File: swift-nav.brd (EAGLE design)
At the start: 53 x 53 mm, 171 parts, among them J1 SMA_EDGE, J6 ZX62-B-5PA, Q1 MOSFET-PCHANNELSMD, U1 6SLX9FTG256, U10 MAX2769, U12 PT7M8206B33TA5EX, U13 M25PX80, U2 LTC3407A_DFN, U3 STM32-M-64-LQFP, U4 7Q-16.368MBG-T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

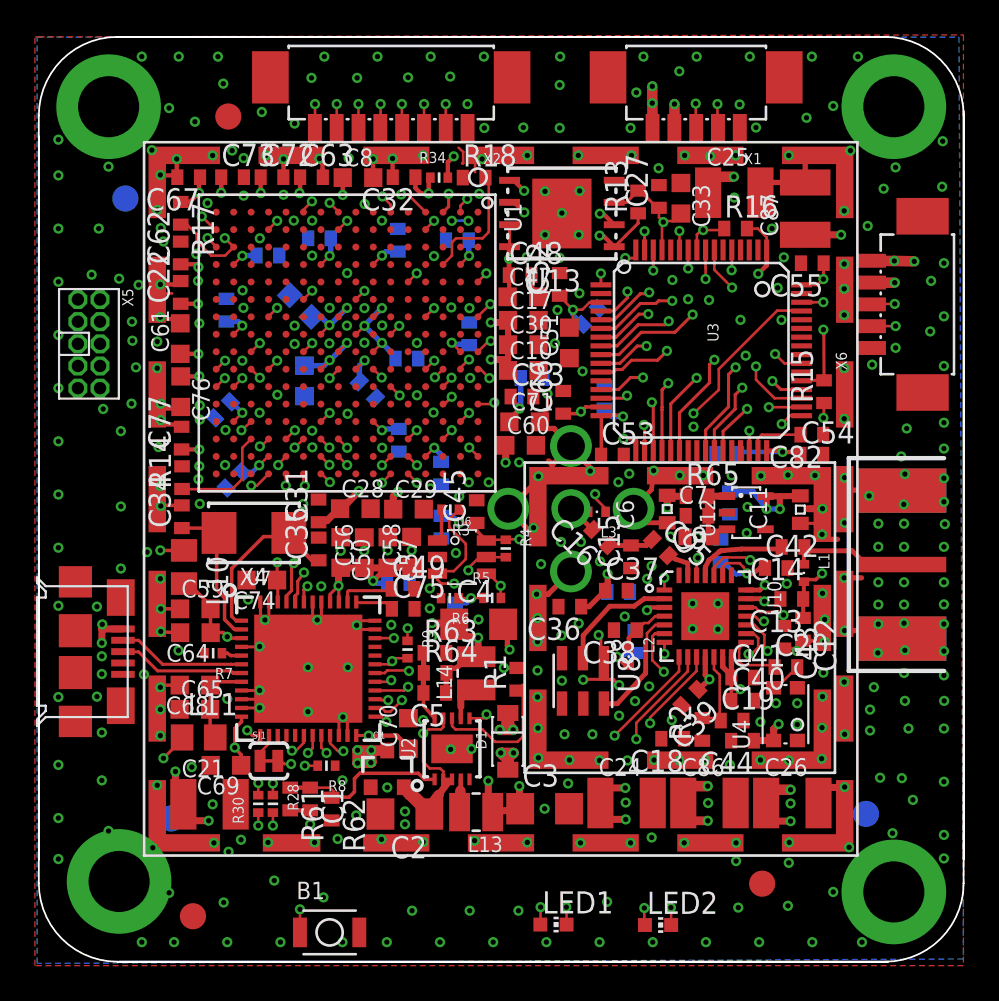
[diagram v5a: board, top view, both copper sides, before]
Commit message: Changed hole separation to 43.8mm
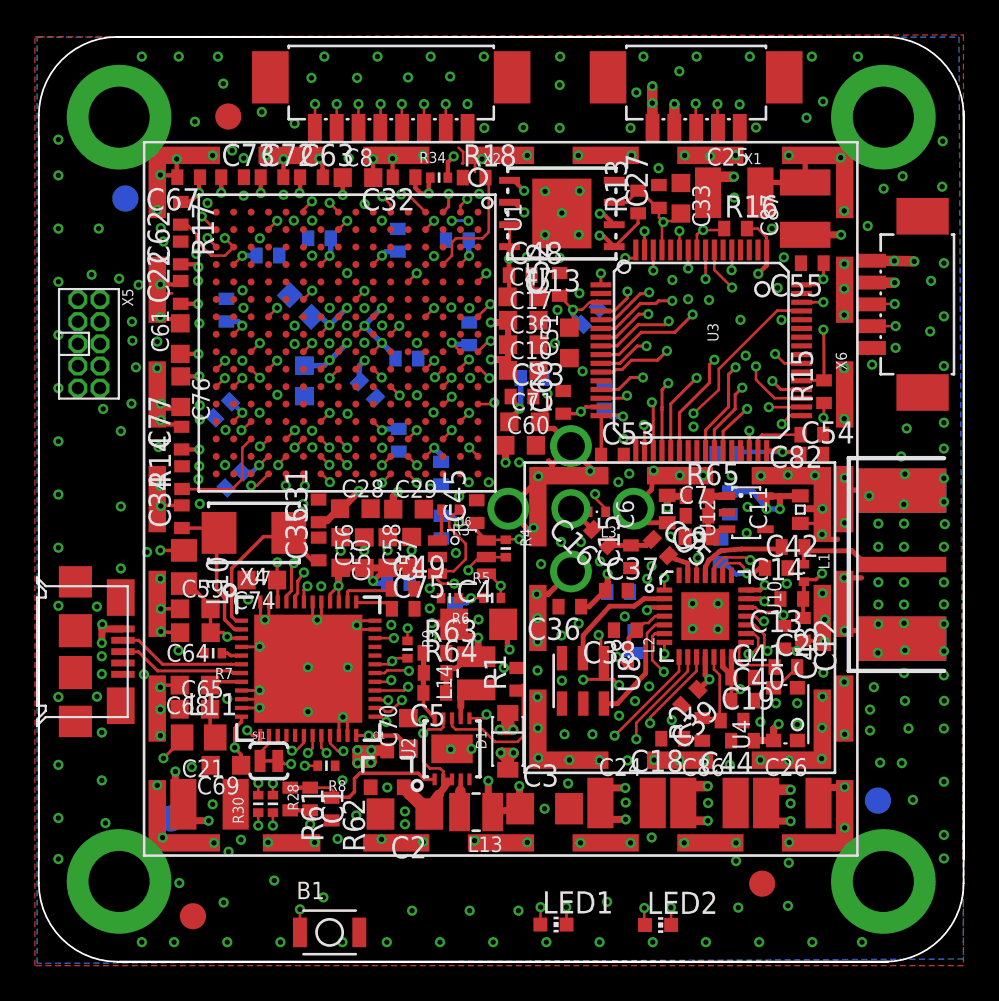
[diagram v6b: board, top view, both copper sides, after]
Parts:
- moved JP5 1.03 mm to (51.5, 12.6)
- moved H4 0.85 mm to (51.8, 51.8)
- moved H2 0.85 mm to (51.8, 8.00)
- moved H3 0.85 mm to (8.00, 51.8)
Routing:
- net N$39: track 62.6 -> 63.6 mm
- net N$59: track 56.9 -> 57.6 mm
- net GND: vias 403 -> 398
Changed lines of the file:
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@@
 <element name="R28" library="pel_dipol_comp" package="0402-RES" value="150" x="16.8148" y="12.446" rot="R270"/>
 <element name="R30" library="pel_dipol_comp" package="0402-RES" value="150" x="15.9766" y="12.446" rot="R90"/>
-<element name="JP5" library="aspirin" package="FIDUCIAL-1.5X3" value="FIDUCIAL1.5X3" x="50.804" y="11.872" rot="MR180"/>
+<element name="JP5" library="aspirin" package="FIDUCIAL-1.5X3" value="FIDUCIAL1.5X3" x="51.4898" y="12.634" rot="MR180"/>
 <element name="JP6" library="aspirin" package="FIDUCIAL-1.5X3" value="FIDUCIAL1.5X3" x="8.3586" y="47.138" rot="MR270"/>
 <element name="JP7" library="aspirin" package="FIDUCIAL-1.5X3" value="FIDUCIAL1.5X3" x="10.984" y="11.61" rot="MR270"/>
@@
 <element name="X2" library="pel_molex" package="PB-53261-08" value="" x="23.5966" y="52.2832" rot="R180"/>
 <element name="C74" library="rcl" package="C0603K" value="0.047uF" x="16.1798" y="25.273" rot="R180"/>
-<element name="H2" library="swift-nav" package="M3-PAD" value="MOUNT-PAD-ROUNDM3" x="52.4" y="7.4"/>
-<element name="H3" library="swift-nav" package="M3-PAD" value="MOUNT-PAD-ROUNDM3" x="7.4" y="52.4"/>
-<element name="H4" library="swift-nav" package="M3-PAD" value="MOUNT-PAD-ROUNDM3" x="52.4" y="52.4"/>
+<element name="H2" library="swift-nav" package="M3-PAD" value="MOUNT-PAD-ROUNDM3" x="51.8" y="8"/>
+<element name="H3" library="swift-nav" package="M3-PAD" value="MOUNT-PAD-ROUNDM3" x="8" y="51.8"/>
+<element name="H4" library="swift-nav" package="M3-PAD" value="MOUNT-PAD-ROUNDM3" x="51.8" y="51.8"/>
 <element name="R8" library="pel_dipol_comp" package="0402-RES" value="10K" x="19.8824" y="14.6354" rot="R180"/>
 <element name="SJ1" library="SparkFun-Passives" package="SJ_2S-TRACE" value="SOLDERJUMPERTRACE" x="16.5862" y="14.9098"/>
@@
 <via x="11.4172" y="55.2704" extent="1-16" drill="0.3"/>
 <via x="9.301" y="55.2704" extent="1-16" drill="0.3"/>
-<via x="7.3944" y="48.965" extent="1-16" drill="0.3"/>
-<via x="10.8664" y="52.3224" extent="1-16" drill="0.3"/>
 <via x="55.2004" y="50.4222" extent="1-16" drill="0.3"/>
-<via x="52.4986" y="48.9252" extent="1-16" drill="0.3"/>
-<via x="48.9252" y="52.4414" extent="1-16" drill="0.3"/>
-<via x="48.9252" y="7.3994" extent="1-16" drill="0.3"/>
-<via x="52.324" y="10.7648" extent="1-16" drill="0.3"/>
-<via x="49.8348" y="9.9568" extent="1-16" drill="0.3"/>
-<via x="9.9314" y="9.9314" extent="1-16" drill="0.3"/>
-<via x="10.8664" y="7.3486" extent="1-16" drill="0.3"/>
-<via x="7.3946" y="10.8918" extent="1-16" drill="0.3"/>
-<via x="9.8806" y="49.911" extent="1-16" drill="0.3"/>
-<via x="49.911" y="49.8856" extent="1-16" drill="0.3"/>
+<via x="52.905" y="48.4172" extent="1-16" drill="0.3"/>
+<via x="48.341" y="52.6954" extent="1-16" drill="0.3"/>
+<via x="49.5808" y="11.0744" extent="1-16" drill="0.3"/>
+<via x="10.4902" y="10.5156" extent="1-16" drill="0.3"/>
+<via x="11.4506" y="7.9074" extent="1-16" drill="0.3"/>
+<via x="7.2168" y="11.349" extent="1-16" drill="0.3"/>
+<via x="49.3522" y="49.4792" extent="1-16" drill="0.3"/>
 <polygon width="0.1524" layer="15">
 <vertex x="3.302" y="56.388"/>
@@
 <wire x1="31.7" y1="42" x2="31.7" y2="42.7" width="0.2032" layer="1"/>
 <contactref element="H5" pad="B3,0"/>
-<wire x1="9.9314" y1="9.9314" x2="8" y2="8" width="0" layer="19" extent="1-1"/>
 </signal>
 <signal name="N$3">
@@
 <wire x1="52.4256" y1="43.561" x2="53.5686" y2="43.5356" width="0.6096" layer="1"/>
 <wire x1="38.5572" y1="52.6034" x2="38.5572" y2="53.5686" width="0.6096" layer="15"/>
-<wire x1="38.5572" y1="53.5686" x2="44.323" y2="53.4924" width="0.6096" layer="15"/>
-<wire x1="44.323" y1="53.4924" x2="53.5686" y2="44.2468" width="0.6096" layer="15"/>
-<wire x1="53.5686" y1="44.2468" x2="53.5686" y2="43.5356" width="0.6096" layer="15"/>
+<wire x1="38.5572" y1="53.5686" x2="44.1706" y2="53.5432" width="0.6096" layer="15"/>
+<wire x1="44.1706" y1="53.5432" x2="53.5686" y2="44.1452" width="0.6096" layer="15"/>
+<wire x1="53.5686" y1="44.1452" x2="53.5686" y2="43.5356" width="0.6096" layer="15"/>
 <wire x1="53.5686" y1="43.5356" x2="52.4256" y2="43.561" width="0.6096" layer="15"/>
 <wire x1="53.5686" y1="43.5356" x2="53.5686" y2="35.1028" width="0.6096" layer="15"/>
 <wire x1="54.4068" y1="33.02" x2="54.4068" y2="12.3952" width="0.6096" layer="15"/>
-<wire x1="46.6598" y1="8.1534" x2="39.5224" y2="8.1534" width="0.6096" layer="15"/>
+<wire x1="47.8028" y1="8.1534" x2="39.5224" y2="8.1534" width="0.6096" layer="15"/>
 <wire x1="39.5224" y1="8.1534" x2="38.4302" y2="9.2456" width="0.6096" layer="15"/>
 <wire x1="38.4302" y1="9.2456" x2="27.7368" y2="9.2456" width="0.6096" layer="15"/>
@@
 <wire x1="22.4282" y1="15.5194" x2="21.717" y2="15.5194" width="0.6096" layer="15"/>
 <wire x1="51.181" y1="33.02" x2="54.4068" y2="33.02" width="0.4064" layer="15"/>
-<wire x1="46.6598" y1="8.1534" x2="50.1142" y2="11.6078" width="0.6096" layer="15"/>
-<wire x1="50.1142" y1="11.6078" x2="53.6194" y2="11.6078" width="0.6096" layer="15"/>
 <wire x1="53.6194" y1="11.6078" x2="54.4068" y2="12.3952" width="0.6096" layer="15"/>
 <wire x1="53.5686" y1="35.1028" x2="54.4068" y2="34.2646" width="0.6096" layer="15"/>
@@
 <wire x1="51.1478" y1="43.5718" x2="51.1556" y2="43.564" width="0.6096" layer="1"/>
 <wire x1="51.1556" y1="43.564" x2="51.1556" y2="43.561" width="0.6096" layer="1"/>
+<wire x1="47.8028" y1="8.1534" x2="51.2572" y2="11.6078" width="0.6096" layer="15"/>
+<wire x1="51.2572" y1="11.6078" x2="53.6194" y2="11.6078" width="0.6096" layer="15"/>
 </signal>
 <signal name="SPI2NSS_FPGA">
@@
 <wire x1="39.6374" y1="6.4382" x2="39.624" y2="6.5024" width="0.1524" layer="1"/>
 <via x="39.624" y="6.5024" extent="1-16" drill="0.3"/>
-<wire x1="46.1772" y1="7.239" x2="52.8574" y2="13.9192" width="0.1524" layer="2"/>
-<via x="52.8574" y="13.9192" extent="1-16" drill="0.3"/>
-<wire x1="52.8574" y1="13.9192" x2="52.3748" y2="14.4018" width="0.1524" layer="15"/>
-<wire x1="52.3748" y1="14.4018" x2="52.3748" y2="30.5054" width="0.1524" layer="15"/>
+<via x="52.8574" y="14.7828" extent="1-16" drill="0.3"/>
+<wire x1="52.8574" y1="14.7828" x2="52.3748" y2="15.2654" width="0.1524" layer="15"/>
+<wire x1="52.3748" y1="15.2654" x2="52.3748" y2="30.5054" width="0.1524" layer="15"/>
 <wire x1="52.3748" y1="30.5054" x2="49.5808" y2="33.2994" width="0.1524" layer="15"/>
 <wire x1="49.5808" y1="33.2994" x2="48.133" y2="33.2994" width="0.1524" layer="15"/>
@@
 <wire x1="43.3324" y1="43.6118" x2="43.9166" y2="43.0276" width="0.1524" layer="15"/>
 <wire x1="43.9166" y1="43.0276" x2="43.9166" y2="42.7482" width="0.1524" layer="15"/>
-<wire x1="46.1772" y1="7.239" x2="40.3606" y2="7.239" width="0.1524" layer="2"/>
+<wire x1="47.2694" y1="7.239" x2="40.3606" y2="7.239" width="0.1524" layer="2"/>
 <wire x1="40.3606" y1="7.239" x2="39.624" y2="6.5024" width="0.1524" layer="2"/>
+<wire x1="52.8574" y1="14.7828" x2="52.8574" y2="14.7574" width="0.1524" layer="2"/>
+<wire x1="52.8574" y1="14.7828" x2="52.8574" y2="12.827" width="0.1524" layer="2"/>
+<wire x1="52.8574" y1="12.827" x2="47.2694" y2="7.239" width="0.1524" layer="2"/>
 </signal>
 <signal name="MAX_NSHDN">
@@
 <wire x1="33.643" y1="6.3874" x2="33.6296" y2="6.5278" width="0.1524" layer="1"/>
 <via x="33.6296" y="6.5278" extent="1-16" drill="0.3"/>
-<wire x1="46.5836" y1="8.3058" x2="51.5874" y2="13.3096" width="0.1524" layer="2"/>
-<wire x1="51.5874" y1="13.3096" x2="51.6128" y2="13.3096" width="0.1524" layer="2"/>
-<wire x1="51.6128" y1="13.3096" x2="51.6128" y2="13.9446" width="0.1524" layer="2"/>
-<via x="51.6128" y="13.9446" extent="1-16" drill="0.3"/>
-<wire x1="51.6128" y1="13.9446" x2="52.0446" y2="14.3764" width="0.1524" layer="15"/>
-<wire x1="52.0446" y1="14.3764" x2="52.0446" y2="30.3276" width="0.1524" layer="15"/>
+<via x="51.6128" y="14.8082" extent="1-16" drill="0.3"/>
+<wire x1="51.6128" y1="14.8082" x2="52.0446" y2="15.24" width="0.1524" layer="15"/>
+<wire x1="52.0446" y1="15.24" x2="52.0446" y2="30.3276" width="0.1524" layer="15"/>
 <wire x1="47.0916" y1="38.1254" x2="45.9486" y2="39.2684" width="0.1524" layer="15"/>
 <wire x1="45.9486" y1="39.2684" x2="40.9194" y2="39.2684" width="0.1524" layer="15"/>
@@
 <wire x1="48.006" y1="32.9184" x2="49.4538" y2="32.9184" width="0.1524" layer="15"/>
 <wire x1="49.4538" y1="32.9184" x2="52.0446" y2="30.3276" width="0.1524" layer="15"/>
-<wire x1="46.5836" y1="8.3058" x2="35.4076" y2="8.3058" width="0.1524" layer="2"/>
+<wire x1="47.5996" y1="8.3058" x2="35.4076" y2="8.3058" width="0.1524" layer="2"/>
 <wire x1="35.4076" y1="8.3058" x2="33.6296" y2="6.5278" width="0.1524" layer="2"/>
+<wire x1="51.6128" y1="14.8082" x2="51.6128" y2="14.3764" width="0.1524" layer="2"/>
+<wire x1="51.6128" y1="12.319" x2="51.6128" y2="14.8082" width="0.1524" layer="2"/>
+<wire x1="47.5996" y1="8.3058" x2="51.6128" y2="12.319" width="0.1524" layer="2"/>
 </signal>
 <signal name="N$24">
